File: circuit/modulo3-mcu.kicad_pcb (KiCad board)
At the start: 2 copper layers, 23 parts, among them SW1 RST_SW, U1 74LVC2G32DC, U2 AVR64DA64, U3 SN74LVC1G17, Y1 32768Hz

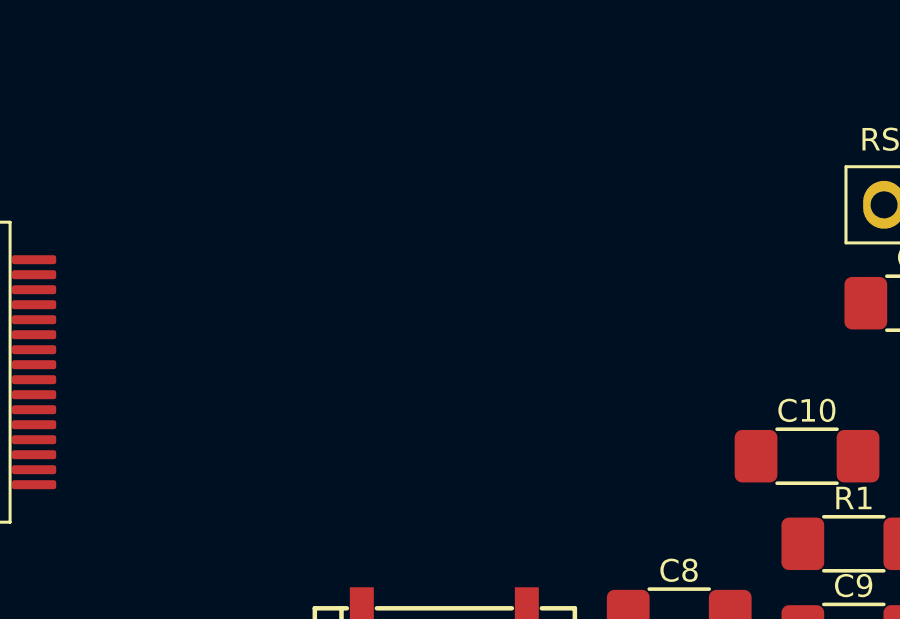
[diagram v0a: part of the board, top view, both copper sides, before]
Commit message: mcu board; fv1 board tracing
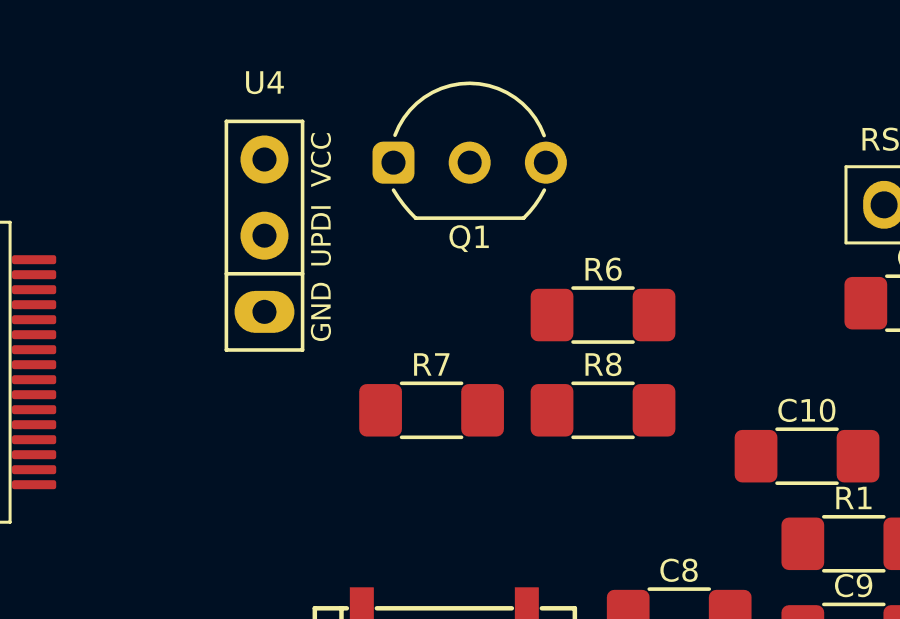
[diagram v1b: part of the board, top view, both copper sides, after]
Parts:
- added Q1: BS250, myAmp:TO-92_Inline_Wide, F.Cu at (118.1, 51.4)
- added R6: 10k, myAmp:C_1206, F.Cu at (122.6, 56.5)
- added R7: 10k, myAmp:C_1206, F.Cu at (116.8, 59.7)
- added R8: 10k, myAmp:C_1206, F.Cu at (122.6, 59.7)
- added U4: UPDI, myAmp:UDPI, F.Cu at (111.3, 53.9)

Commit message: general layout and board sizes
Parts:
- removed C1: 100n, myAmp:C_1206
- removed R1: 330, myAmp:C_1206
- removed SW1: RST_SW, myAmp:Switch_2.5mm
- added C13: 3u3, myAmp:CPOL_D4_P1.5, F.Cu at (119.4, 66.0)
- added C14: 3u3, myAmp:CPOL_D4_P1.5, F.Cu at (114.9, 66.0)
- added C15: 3u3, myAmp:CPOL_D4_P1.5, F.Cu at (110.5, 66.0)
- added R9: 100, myAmp:R_10MM, F.Cu at (102.9, 85.7)
- added U5: TOUCHSCREEN_240x320, myAmp:TOUCHSCREEN_2.8, F.Cu at (92.0, 80.0)
- added U6: FV1_CONN, myAmp:FV1_CONN, F.Cu at (156.8, 57.1)
- added U7: DBG_UART, myAmp:DBG_UART, F.Cu at (126.4, 72.4)
- R2, R3, R4, R5: footprint myAmp:C_1206 -> myAmp:R_10MM
- R6, R7, R8: footprint myAmp:C_1206 -> myAmp:R_1206
- moved C4 47.5 mm to (118.7, 92.1)
- moved C5 47.2 mm to (118.7, 94.6)
- moved C2 41.1 mm to (109.2, 80.6), turned to -90 degrees
- moved Q1 36.1 mm to (106.7, 85.7), turned to -90 degrees
- moved U2 33.2 mm to (120.7, 82.5)
- moved C3 32.5 mm to (111.8, 80.6), turned to -90 degrees
- moved U4 25.1 mm to (129.5, 71.1)
- moved U3 24.2 mm to (150.5, 84.5), turned to 90 degrees
- moved C8 22.0 mm to (133.3, 87.0)
- moved R2 21.7 mm to (147.3, 75.6), turned to -90 degrees
- moved R5 20.7 mm to (152.4, 75.6), turned to -90 degrees
- moved Y1 20.4 mm to (133.3, 80.6)
- moved C6 19.7 mm to (121.9, 73.7), turned to 180 degrees
- moved C9 19.4 mm to (128.9, 86.4), turned to 90 degrees
- moved D1 18.7 mm to (146.1, 84.5)
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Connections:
- U2 pad 1: unconnected-(U2-Pad1) -> /T_IRQ
- U2 pad 10: unconnected-(U2-Pad10) -> /S_CS
- U2 pad 11: unconnected-(U2-Pad11) -> /S_LED
- U2 pad 2: unconnected-(U2-Pad2) -> /S_MOSI
- U2 pad 3: unconnected-(U2-Pad3) -> /S_MISO
- U2 pad 4: unconnected-(U2-Pad4) -> /S_SCK
- U2 pad 5: unconnected-(U2-Pad5) -> /T_CS
- U2 pad 50: Net-(C1-Pad1) -> unconnected-(U2-Pad50)
- U2 pad 52: unconnected-(U2-Pad52) -> /DBG_TX
- U2 pad 62: unconnected-(U2-Pad62) -> /PWM0
- U2 pad 63: unconnected-(U2-Pad63) -> /PWM1
- U2 pad 64: unconnected-(U2-Pad64) -> /PWM2
- U2 pad 8: unconnected-(U2-Pad8) -> /S_DC
- U2 pad 9: unconnected-(U2-Pad9) -> /S_RST
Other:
- board outline added: 100 x 50 mm

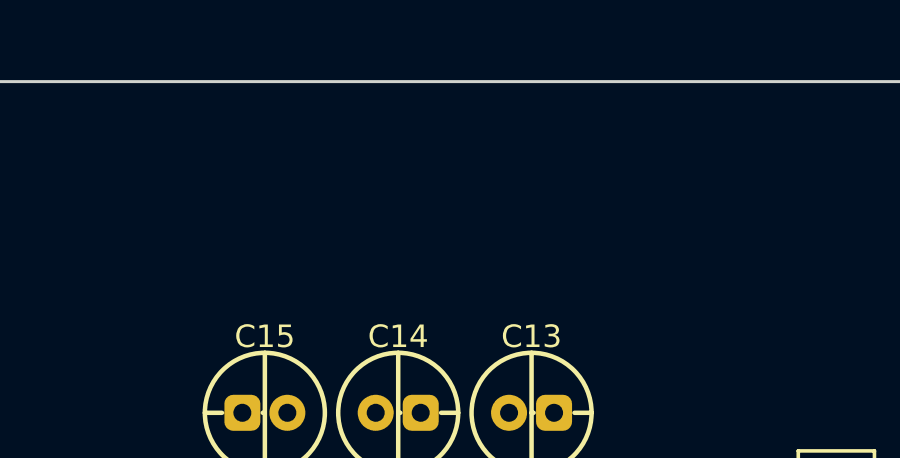
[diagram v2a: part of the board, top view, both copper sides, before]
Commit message: added ampctrl and diffaudio; started changing powamp
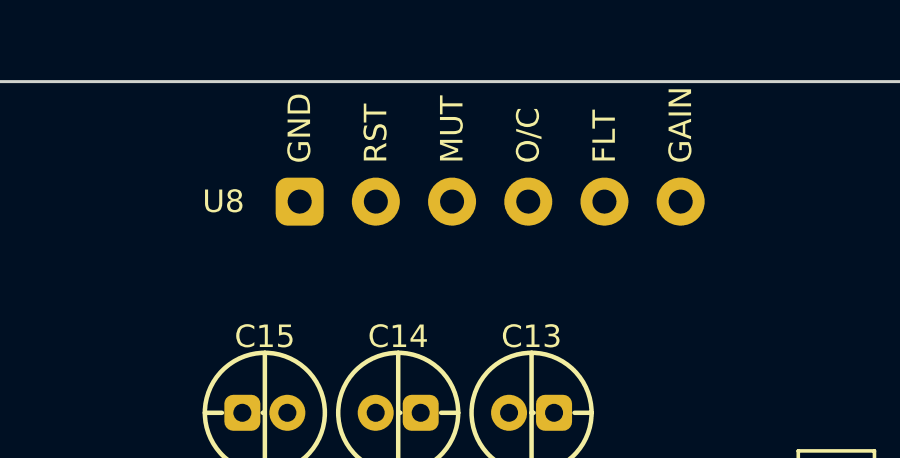
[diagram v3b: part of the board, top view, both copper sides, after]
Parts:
- added U8: AMPCTRL, myAmp:AMPCTRL, F.Cu at (118.0, 59.0)
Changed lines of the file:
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@@
   (net 77 "/FV_SDA")
   (net 78 "/FV_SCL")
+  (net 79 "unconnected-(U8-Pad1)")
+  (net 80 "unconnected-(U8-Pad2)")
+  (net 81 "unconnected-(U8-Pad3)")
+  (net 82 "unconnected-(U8-Pad4)")
+  (net 83 "unconnected-(U8-Pad5)")
+  (net 84 "unconnected-(U8-Pad6)")
   (footprint "myAmp:R_10MM" (layer "F.Cu")
     (at 152.4 75.565 -90)
@@
     )
   )
+  (footprint "myAmp:AMPCTRL" (layer "F.Cu")
+    (at 118 59)
+    (property "Sheetfile" "modulo3-mcu.kicad_sch")
+    (property "Sheetname" "")
+    (attr through_hole)
+    (fp_text reference "U8" (at -8.89 0 unlocked) (layer "F.SilkS")
+      (effects (font (size 0.75 0.75) (thickness 0.15)))
+    )
+    (fp_text value "AMPCTRL" (at 0 1 unlocked) (layer "F.Fab") hide
+      (effects (font (size 1 1) (thickness 0.15)))
+    )
+    (fp_text user "GAIN" (at 6.35 -1.27 90 unlocked) (layer "F.SilkS")
+      (effects (font (size 0.75 0.75) (thickness 0.15)) (justify left))
+    )
+    (fp_text user "FLT" (at 3.81 -1.27 90 unlocked) (layer "F.SilkS")
+      (effects (font (size 0.75 0.75) (thickness 0.15)) (justify left))
+    )
+    (fp_text user "GND" (at -6.35 -1.27 90 unlocked) (layer "F.SilkS")
+      (effects (font (size 0.75 0.75) (thickness 0.15)) (justify left))
+    )
+    (fp_text user "MUT" (at -1.27 -1.27 90 unlocked) (layer "F.SilkS")
+      (effects (font (size 0.75 0.75) (thickness 0.15)) (justify left))
+    )
+    (fp_text user "RST" (at -3.81 -1.27 90 unlocked) (layer "F.SilkS")
+      (effects (font (size 0.75 0.75) (thickness 0.15)) (justify left))
+    )
+    (fp_text user "O/C" (at 1.27 -1.27 90 unlocked) (layer "F.SilkS")
+      (effects (font (size 0.75 0.75) (thickness 0.15)) (justify left))
+    )
+    (pad "1" thru_hole roundrect (at -6.35 0) (size 1.6 1.6) (drill 0.8) (layers *.Cu *.Mask) (roundrect_rratio 0.25)
+      (net 79 "unconnected-(U8-Pad1)") (pinfunction "GND") (pintype "input"))
+    (pad "2" thru_hole circle (at -3.81 0) (size 1.6 1.6) (drill 0.8) (layers *.Cu *.Mask)
+      (net 80 "unconnected-(U8-Pad2)") (pinfunction "RESET") (pintype "input"))
+    (pad "3" thru_hole circle (at -1.27 0) (size 1.6 1.6) (drill 0.8) (layers *.Cu *.Mask)
+      (net 81 "unconnected-(U8-Pad3)") (pinfunction "MUTE") (pintype "input"))
+    (pad "4" thru_hole circle (at 1.27 0) (size 1.6 1.6) (drill 0.8) (layers *.Cu *.Mask)
+      (net 82 "unconnected-(U8-Pad4)") (pinfunction "OTW_CLIP") (pintype "output"))
+    (pad "5" thru_hole circle (at 3.81 0) (size 1.6 1.6) (drill 0.8) (layers *.Cu *.Mask)
+      (net 83 "unconnected-(U8-Pad5)") (pinfunction "FAULT") (pintype "output"))
+    (pad "6" thru_hole circle (at 6.35 0) (size 1.6 1.6) (drill 0.8) (layers *.Cu *.Mask)
+      (net 84 "unconnected-(U8-Pad6)") (pinfunction "GAINSEL") (pintype "output"))
+    (model "${KIPRJMOD}/myAmp.pretty/models/PinHeader_1x06_P2.54mm_Vertical.wrl"
+      (offset (xyz 6.35 0 0))
+      (scale (xyz 1 1 1))
+      (rotate (xyz 0 0 90))
+    )
+  )

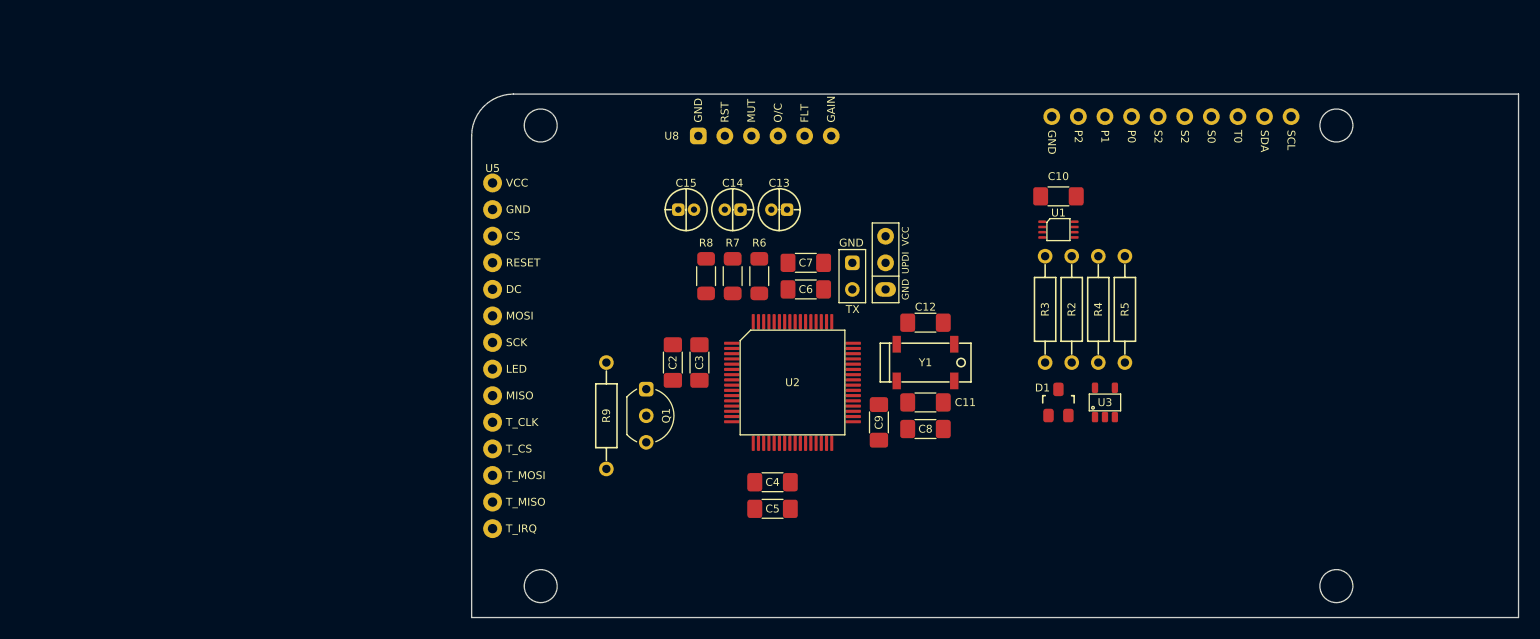
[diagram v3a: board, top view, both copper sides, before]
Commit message: got the pcs and holes sizes for mcu, poweamp and fv1
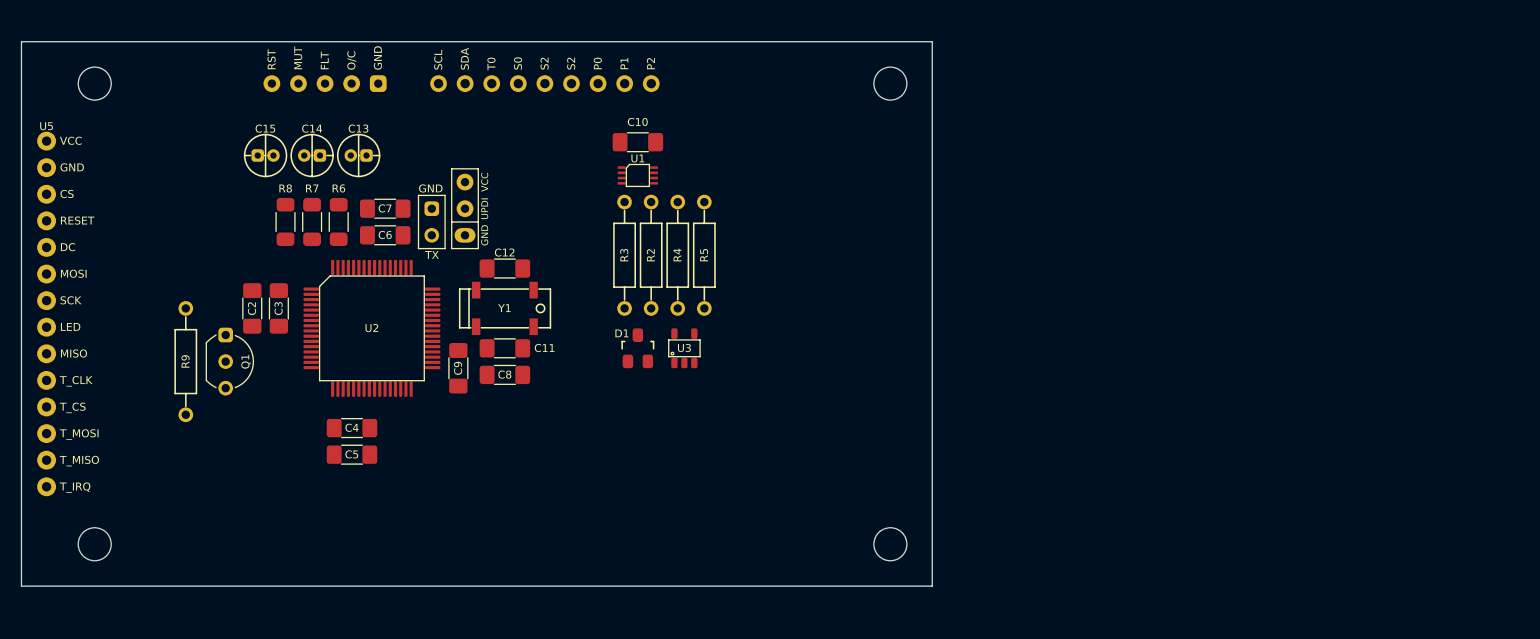
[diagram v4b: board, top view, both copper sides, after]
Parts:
- moved U6 59.9 mm to (97.0, 54.0), turned to 0 degrees
- moved U5 42.8 mm to (49.4, 76.0)
- moved U8 42.3 mm to (76.0, 54.0)
- moved C10 40.5 mm to (105.9, 59.6)
- moved C14 40.5 mm to (74.8, 60.9)
- moved C3 40.5 mm to (71.6, 75.5)
- moved C4 40.5 mm to (78.6, 86.9)
- moved C5 40.5 mm to (78.6, 89.4)
- moved D1 40.5 mm to (105.9, 79.3)
- moved Q1 40.5 mm to (66.5, 80.6)
- moved R4 40.5 mm to (109.7, 70.4)
- moved R5 40.5 mm to (112.2, 70.4)
- moved R7 40.5 mm to (74.8, 67.2)
- moved U1 40.5 mm to (105.9, 62.8)
- moved U2 40.5 mm to (80.5, 77.4)
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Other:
- board size 100 x 50 mm -> 87 x 52 mm

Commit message: fv-1 mostly done; power progressed
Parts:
- added U10: PWR_CONN, myAmp:PWR_CONN, F.Cu at (121.0, 54.0)
- added U9: ~, myAmp:PREAMP_CONN, F.Cu at (80.0, 98.0)
- moved U6 4.00 mm to (101.0, 54.0)
- moved R5 1.44 mm to (113.7, 70.5)
- moved R4 0.81 mm to (110.5, 70.5)
- moved R3 0.48 mm to (104.1, 70.5)
- moved R2 0.19 mm to (107.3, 70.5)
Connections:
- U6 pad 10: /FV_SCL -> /FV_CLIP
- U6 pad 2: /POT2 -> /POT1
- U6 pad 3: /POT1 -> /POT0
- U6 pad 4: /POT0 -> /S2
- U6 pad 5: /S2 -> /S1
- U6 pad 6: /S1 -> /S0
- U6 pad 7: /S0 -> /FV_SDA
- U6 pad 8: /T0 -> /FV_SCL
- U6 pad 9: /FV_SDA -> /T0

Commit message: lotsa things :)
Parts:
- added C1: 10n, myAmp:C_1206, F.Cu at (124.5, 69.8)
- added Q2: BS170, myAmp:TO-92_Inline_Wide, F.Cu at (63.5, 64.8)
- added R1: 10k, myAmp:R_10MM, F.Cu at (120.7, 61.6)
- added R10: 1k, myAmp:R_10MM, F.Cu at (120.7, 74.3)
- added R11: 10k, myAmp:R_10MM, F.Cu at (73.7, 61.6)
- added R12: 100, myAmp:R_10MM, F.Cu at (71.1, 61.6)
- added R13: 100, myAmp:R_10MM, F.Cu at (78.7, 61.6)
- added R14: 100, myAmp:R_10MM, F.Cu at (76.2, 61.6)
- added R15: 10k, myAmp:R_10MM, F.Cu at (63.5, 51.4)
- added U11: FOOTSWITCH, myAmp:FOOTSWITCH, F.Cu at (111.8, 83.2)
- added U12: ~, myAmp:KNOBS, F.Cu at (125.1, 88.9)
- R6, R7, R8: footprint myAmp:R_1206 -> myAmp:R_10MM
- moved U7 27.1 mm to (95.2, 92.7)
- moved C15 13.2 mm to (83.2, 57.8), turned to 90 degrees
- moved C14 13.1 mm to (87.5, 57.8)
- moved C13 12.2 mm to (91.3, 59.7)
- moved R6 11.0 mm to (88.3, 66.0)
- moved R7 11.0 mm to (85.7, 66.0)
- moved R8 11.0 mm to (83.2, 66.0)
- moved Q1 8.36 mm to (61.0, 74.3), turned to 0 degrees
- moved U4 7.73 mm to (88.9, 73.7), turned to 180 degrees
- moved C4 7.09 mm to (78.1, 94.0)
- moved C8 6.86 mm to (90.8, 88.3), turned to -90 degrees
- moved C7 6.27 mm to (79.4, 71.8)
- moved C2 5.29 mm to (67.9, 80.6)
- moved C3 5.29 mm to (70.5, 80.6)
- moved C11 4.85 mm to (95.2, 83.7)
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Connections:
- U10 pad 1: unconnected-(U10-GND-Pad1) -> GND
- U10 pad 2: unconnected-(U10-30V-Pad2) -> Net-(U10-30V)
- U10 pad 3: unconnected-(U10-5V-Pad3) -> +5V
- U2 pad 1: /T_IRQ -> unconnected-(U2-PA3-Pad1)
- U2 pad 10: /S_CS -> unconnected-(U2-PB2-Pad10)
- U2 pad 11: /S_LED -> unconnected-(U2-PB3-Pad11)
- U2 pad 12: unconnected-(U2-PB4-Pad12) -> /S_MOSI
- U2 pad 13: unconnected-(U2-PB5-Pad13) -> /S_MISO
- U2 pad 14: unconnected-(U2-PB6-Pad14) -> /S_SCK
- U2 pad 15: unconnected-(U2-PB7-Pad15) -> /T_IRQ
- U2 pad 18: unconnected-(U2-PC2-Pad18) -> /MIX_SDA
- U2 pad 19: unconnected-(U2-PC3-Pad19) -> /MIX_SCL
- U2 pad 2: /S_MOSI -> unconnected-(U2-PA4-Pad2)
- U2 pad 3: /S_MISO -> unconnected-(U2-PA5-Pad3)
- U2 pad 4: /S_SCK -> unconnected-(U2-PA6-Pad4)
- U2 pad 46: unconnected-(U2-PF2-Pad46) -> /FV_SDA
- U2 pad 47: unconnected-(U2-PF3-Pad47) -> /FV_SCL
- U2 pad 48: unconnected-(U2-PF4-Pad48) -> /S0
- U2 pad 49: unconnected-(U2-PF5-Pad49) -> /S1
- U2 pad 5: /T_CS -> unconnected-(U2-PA7-Pad5)
- U2 pad 50: unconnected-(U2-(~{RESET})PF6-Pad50) -> /S2
- U2 pad 52: /DBG_TX -> /PWM0
- U2 pad 53: unconnected-(U2-PG1-Pad53) -> /PWM1
- U2 pad 54: unconnected-(U2-PG2-Pad54) -> /PWM2
- U2 pad 58: unconnected-(U2-PG4-Pad58) -> /OTW_CLIP
- U2 pad 59: unconnected-(U2-PG5-Pad59) -> /FAULT
- U2 pad 60: unconnected-(U2-PG6-Pad60) -> /POW_RESET
- U2 pad 62: /PWM0 -> unconnected-(U2-PA0(EXTCLK)-Pad62)
- U2 pad 63: /PWM1 -> unconnected-(U2-PA1-Pad63)
- U2 pad 64: /PWM2 -> unconnected-(U2-PA2-Pad64)
- U2 pad 8: /S_DC -> unconnected-(U2-PB0-Pad8)
- U2 pad 9: /S_RST -> unconnected-(U2-PB1-Pad9)
- U5 pad 1: /T_IRQ -> +3.3V
- U5 pad 10: /S_DC -> /S_SCK
- U5 pad 11: /S_RST -> /T_CS
- U5 pad 12: /S_CS -> /S_MOSI
- U5 pad 13: GND -> /S_MISO
- U5 pad 14: +3.3V -> /T_IRQ
- U5 pad 2: /S_MISO -> GND
- U5 pad 3: /S_MOSI -> /S_CS
- U5 pad 4: /T_CS -> /S_RST
- U5 pad 5: /S_SCK -> /S_DC
- U5 pad 6: /S_MISO -> /S_MOSI
- U5 pad 7: Net-(U5-LED) -> /S_SCK
- U5 pad 8: /S_SCK -> Net-(U5-LED)
- U5 pad 9: /S_MOSI -> /S_MISO
- U8 pad 1: unconnected-(U8-GND-Pad1) -> GND
- U8 pad 2: unconnected-(U8-RESET-Pad2) -> Net-(U8-RESET)
- U8 pad 3: unconnected-(U8-MUTE-Pad3) -> /MUTE
- U8 pad 4: unconnected-(U8-FAULT-Pad4) -> Net-(U8-FAULT)
- U8 pad 5: unconnected-(U8-OTW_CLIP-Pad5) -> Net-(U8-OTW_CLIP)
- U9 pad 1: unconnected-(U9-SDA-Pad1) -> /MIX_SDA
- U9 pad 2: unconnected-(U9-SCL-Pad2) -> /MIX_SCL
- U9 pad 3: unconnected-(U9-GND-Pad3) -> GND
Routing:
- net /S_MOSI: track 0.00 -> 43.2 mm
- net /S_MISO: track 0.00 -> 38.4 mm
- net /S_SCK: track 0.00 -> 8.63 mm
- added copper zone on B.Cu, net GND
- added copper zone on F.Cu, net GND

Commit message: routing mcu
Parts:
- moved U11 24.5 mm to (130.2, 67.0), turned to 0 degrees
- moved U12 7.67 mm to (130.0, 83.0), turned to 90 degrees
- moved Q2 6.54 mm to (66.7, 59.1), turned to -90 degrees
- moved U4 5.43 mm to (90.8, 68.6), turned to 0 degrees
- moved R11 5.08 mm to (78.7, 61.6)
- moved R4 4.84 mm to (113.7, 72.4)
- moved U3 4.84 mm to (114.8, 81.2)
- moved C10 4.84 mm to (110.3, 61.5)
- moved D1 4.84 mm to (110.3, 81.2)
- moved R2 4.84 mm to (111.1, 72.4)
- moved R3 4.84 mm to (108.6, 72.4)
- moved R5 4.84 mm to (116.2, 72.4)
- moved U1 4.84 mm to (110.3, 64.8)
- moved C9 3.81 mm to (88.3, 89.5), turned to -90 degrees
- moved U7 3.18 mm to (95.2, 95.9)
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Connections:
- C10 pad 1: Net-(U1C-VCC) -> +3.3V
- R12 pad 2: /POW_RESET -> /PA_RESET
- U1 pad 8: Net-(U1C-VCC) -> +3.3V
- U2 pad 10: unconnected-(U2-PB2-Pad10) -> /S_DC
- U2 pad 11: unconnected-(U2-PB3-Pad11) -> /T_CS
- U2 pad 5: unconnected-(U2-PA7-Pad5) -> /S_LED
- U2 pad 58: /OTW_CLIP -> unconnected-(U2-PG4-Pad58)
- U2 pad 59: /FAULT -> unconnected-(U2-PG5-Pad59)
- U2 pad 60: /POW_RESET -> unconnected-(U2-PG6-Pad60)
- U2 pad 61: unconnected-(U2-PG7-Pad61) -> /OTW_CLIP
- U2 pad 62: unconnected-(U2-PA0(EXTCLK)-Pad62) -> /FAULT
- U2 pad 63: unconnected-(U2-PA1-Pad63) -> /PA_RESET
- U2 pad 64: unconnected-(U2-PA2-Pad64) -> /MUTE_CTRL
- U2 pad 8: unconnected-(U2-PB0-Pad8) -> /S_CS
- U2 pad 9: unconnected-(U2-PB1-Pad9) -> /S_RST
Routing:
- net /FV_SDA: track 0.00 -> 41.2 mm
- net /S_SCK: track 8.63 -> 46.9 mm
- net /MUTE_CTRL: track 0.00 -> 34.1 mm
- net /FV_SCL: track 0.00 -> 34.1 mm
- net /S_CS: track 0.00 -> 32.9 mm
- net /S0: track 0.00 -> 31.4 mm
- net /S_RST: track 0.00 -> 31.0 mm
- net /S1: track 0.00 -> 31.0 mm
- net /S_DC: track 0.00 -> 30.2 mm
- net /S2: track 0.00 -> 30.2 mm
- net /T_IRQ: track 0.00 -> 27.9 mm
- net /T_CS: track 0.00 -> 25.5 mm
- net +3.3V: track 0.00 -> 16.8 mm
- net /UPDI: track 0.00 -> 15.7 mm
- net /S_LED: track 0.00 -> 14.4 mm
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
